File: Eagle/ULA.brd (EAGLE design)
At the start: 23.5 x 55.1 mm, 5 parts, among them IC1 EPM7128, IC2 Soquete ULA

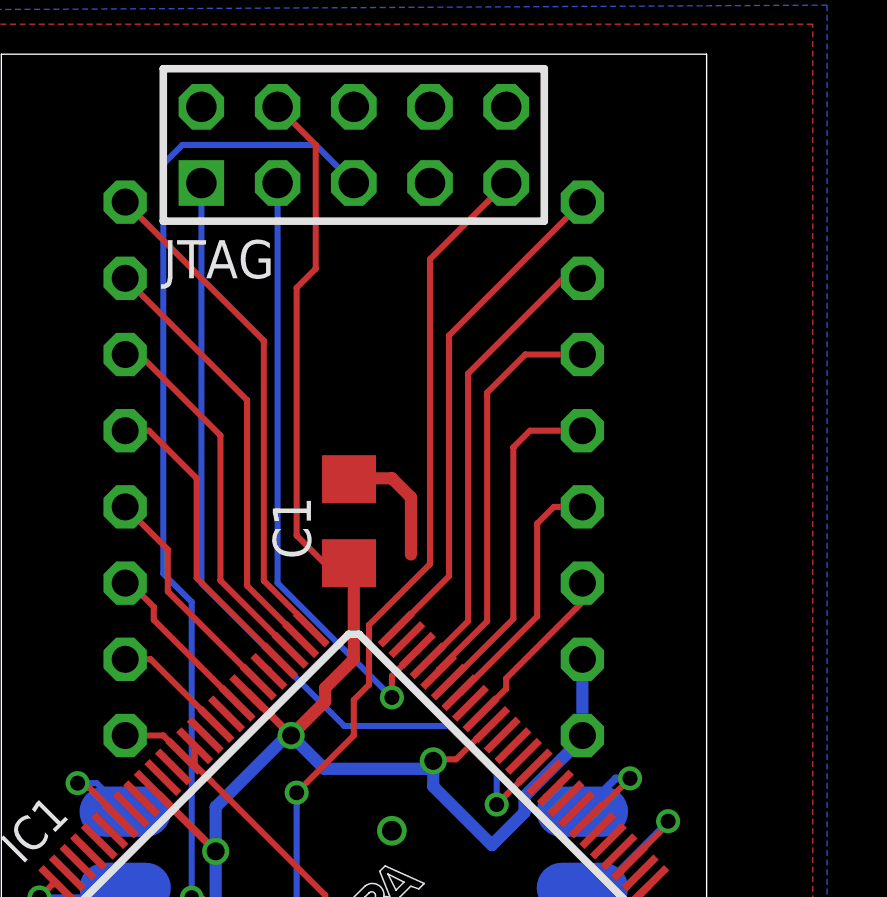
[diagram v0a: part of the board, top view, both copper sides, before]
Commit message: added filters for PWM
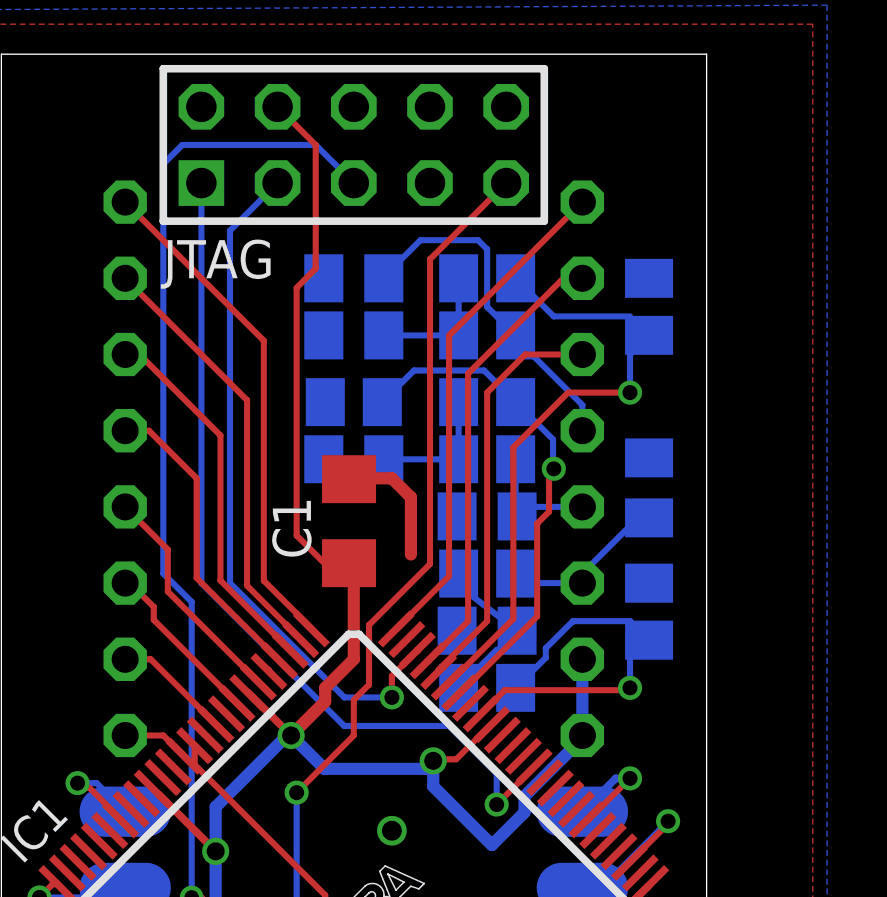
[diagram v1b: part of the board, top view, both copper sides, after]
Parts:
- added C3, C4, C5, C6, C7, C8: (no value), rcl:C0805K
- added R1, R2, R3, R4, R5, R6, R7, R8, R9: (no value), rcl:M0805
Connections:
- new net N$1: C5.1, R4.2, R5.1
- new net N$2: C3.1, R1.2, R2.1
- new net N$3: C4.1, IC2.15, R2.2
- new net N$4: C6.1, IC2.16, R5.2
- new net N$5: C7.1, R7.2, R8.1
- new net N$6: C8.1, IC2.17, R8.2
- net GND: now also C3.2, C4.2, C5.2, C6.2, C7.2, C8.2, R3.1, R6.1, R9.1
- net U: now also R1.1, R3.2; no longer IC2.15
- net V: now also R4.1, R6.2; no longer IC2.16
- net Y: now also R7.1, R9.2; no longer IC2.17
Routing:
- net N$6: track 0.00 -> 9.97 mm
- net Y: track 11.3 -> 19.9 mm, vias 0 -> 1
- net V: track 8.46 -> 16.7 mm, vias 0 -> 1
- net U: track 5.76 -> 12.1 mm, vias 0 -> 1
- net N$2: track 0.00 -> 4.71 mm
- net N$3: track 0.00 -> 4.47 mm
- net N$5: track 0.00 -> 4.40 mm
- net N$1: track 0.00 -> 4.40 mm
- net N$4: track 0.00 -> 3.63 mm
- net TDO: track 20.6 -> 22.9 mm

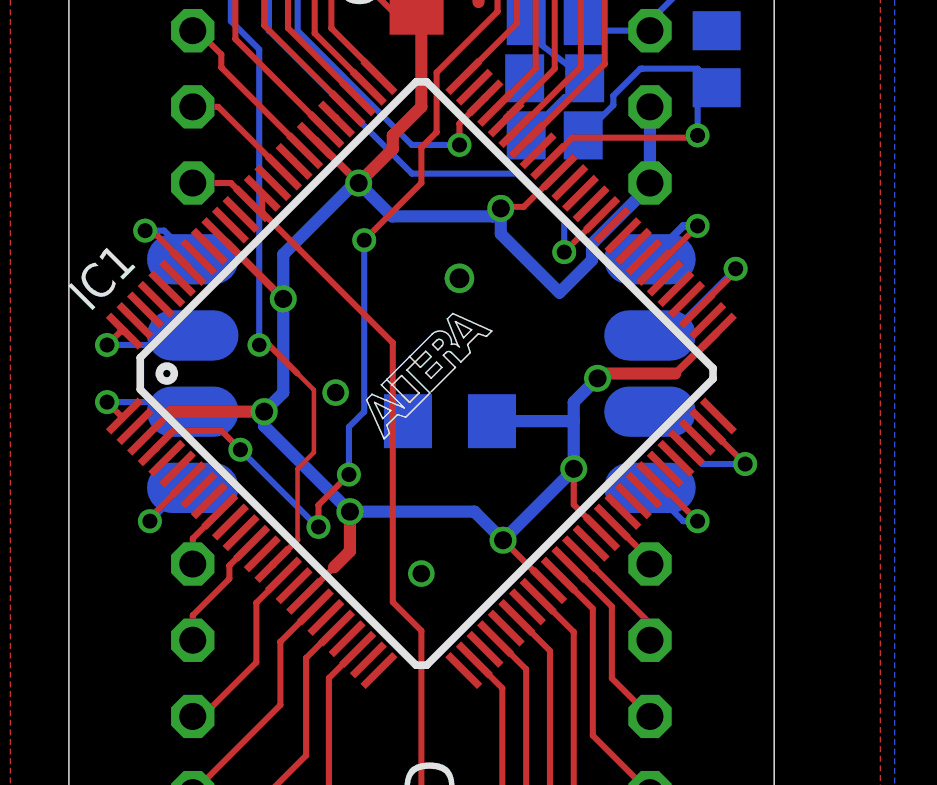
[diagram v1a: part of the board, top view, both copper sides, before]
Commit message: CPLD pinout update
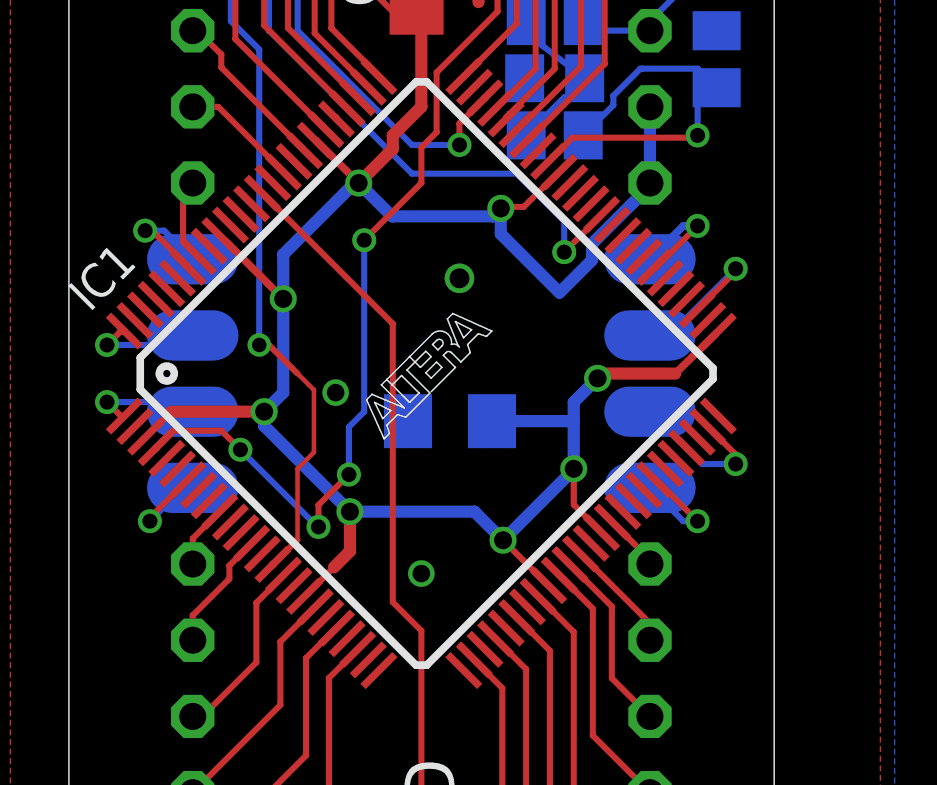
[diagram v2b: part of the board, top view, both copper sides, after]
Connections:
- net SOUND: now also IC1.93; no longer IC1.88
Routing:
- net SOUND: track 2.25 -> 2.87 mm
